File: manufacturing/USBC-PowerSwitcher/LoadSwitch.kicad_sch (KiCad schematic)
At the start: 6 parts, among them Q2 DMP3098LSD

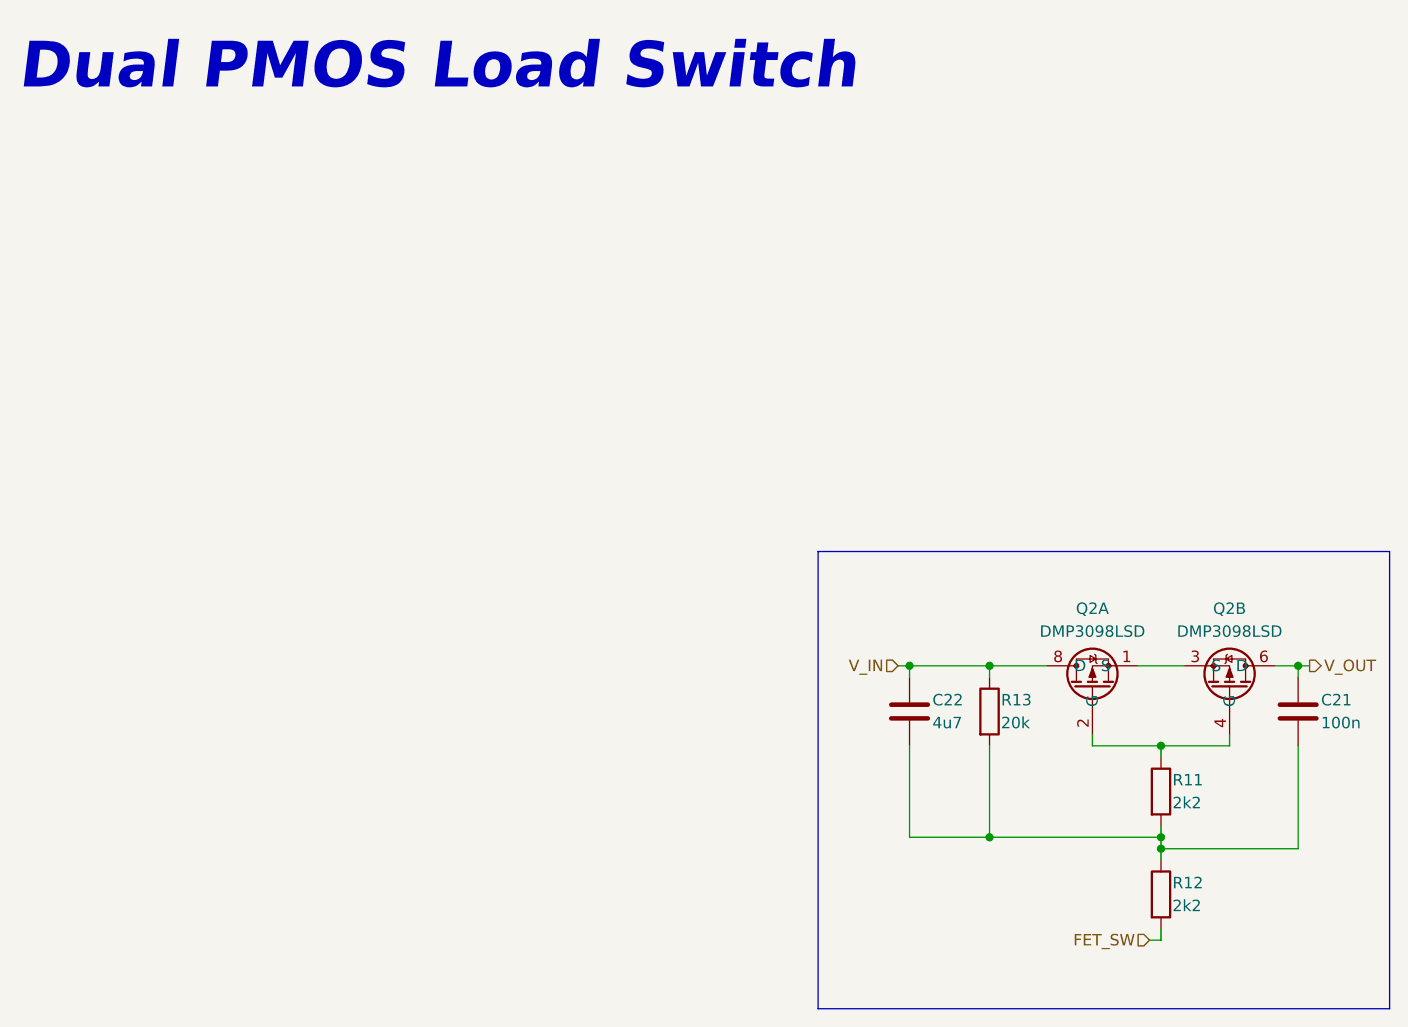
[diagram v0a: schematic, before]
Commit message: First Rough placement
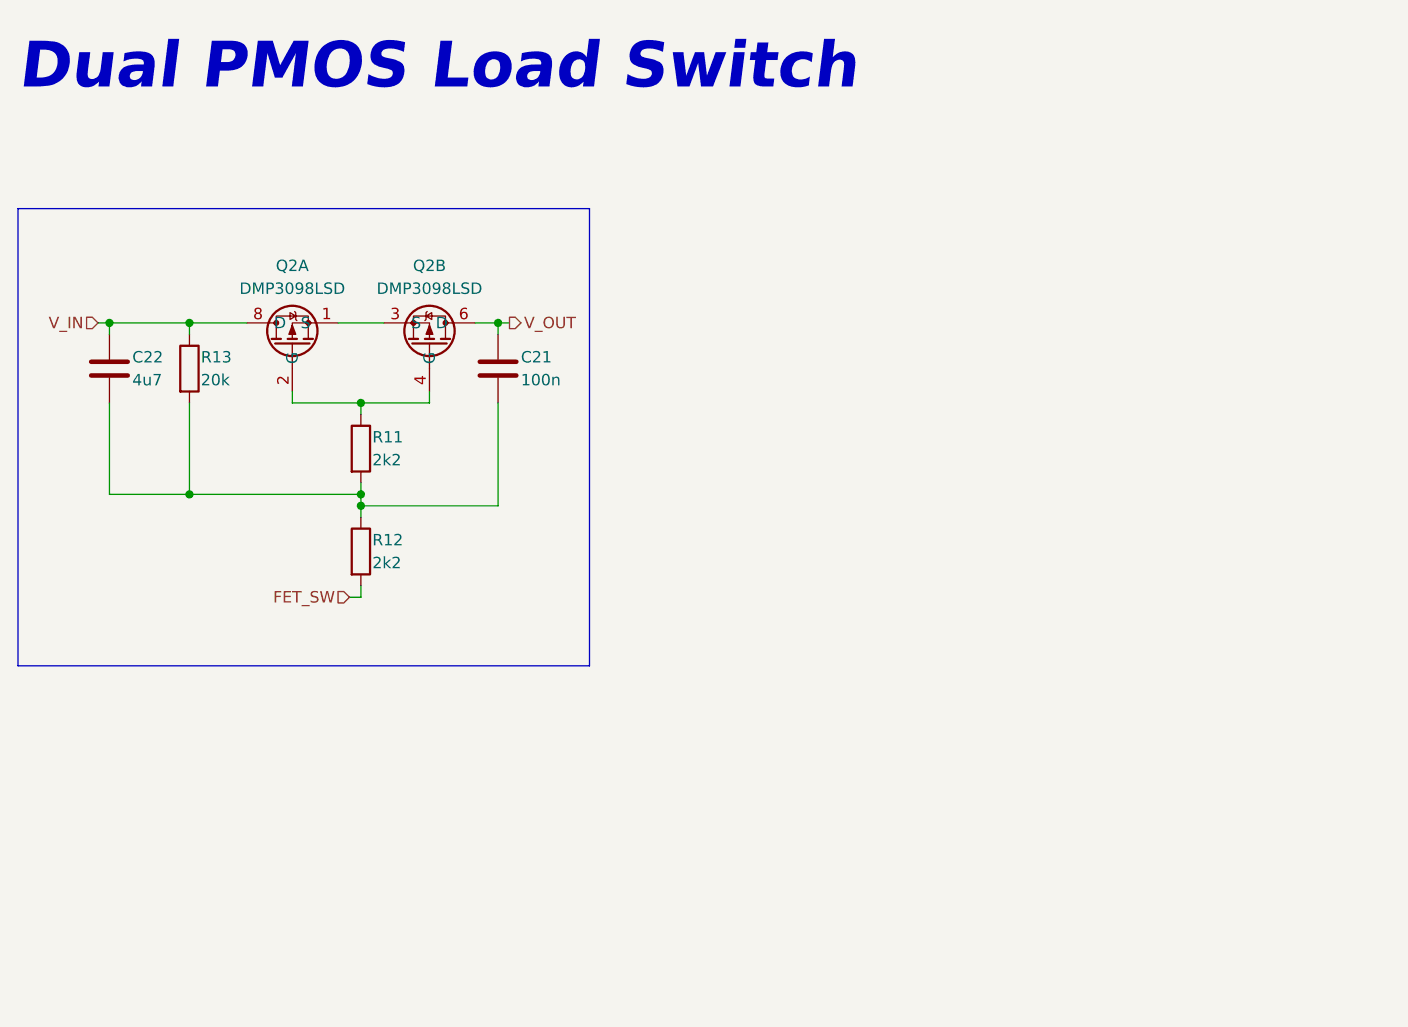
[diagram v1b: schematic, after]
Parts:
- C21: footprint (none) -> Capacitor_SMD:C_0402_1005Metric; LCSC # (none) -> C307331
- C22: footprint (none) -> Capacitor_SMD:C_0805_2012Metric; LCSC # (none) -> C1779
- Q2: footprint (none) -> Package_SO:SO-8_3.9x4.9mm_P1.27mm; LCSC # (none) -> C531177
- R11, R12: footprint (none) -> Resistor_SMD:R_0402_1005Metric; LCSC # (none) -> C25879
- R13: footprint (none) -> Resistor_SMD:R_0402_1005Metric; LCSC # (none) -> C25765
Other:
- moved on the sheet: C21, C22, Q2A, Q2B, R11, R12, R13
